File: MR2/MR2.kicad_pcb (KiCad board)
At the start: 2 copper layers, 14 parts, among them J1 Conn_01x04_Male, J2 Conn_01x04_Male, J3 Conn_01x04_Male, J4 Conn_01x04_Male, J5 Conn_01x02_Male, Q1 2SC1815, U5 LPC1768, U6 MPU6050, U7 R3008SB, U8 MCP2561-E-P

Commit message: update:MR2の基板完成
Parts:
- removed Q1: 2SC1815, Package_TO_SOT_THT:TO-92_Inline
- removed R1, R3: R, Resistor_THT:R_Axial_DIN0207_L6.3mm_D2.5mm_P7.62mm_Horizontal
- removed REF**: universal_B, MyFootprint:universal_B
- removed U6: MPU6050, MyFootprint:MPU6050
- removed U7: R3008SB, MyFootprint:R3008SB
- added J6: Conn_01x02_Male, Connector_JST:JST_XH_S2B-XH-A_1x02_P2.50mm_Horizontal, F.Cu at (109.2, 96.6)
- added J7: Conn_01x04_Male, Connector_JST:JST_XH_S4B-XH-A_1x04_P2.50mm_Horizontal, F.Cu at (108.9, 78.7)
- added J8: Conn_01x02_Male, Connector_JST:JST_XH_S2B-XH-A_1x02_P2.50mm_Horizontal, F.Cu at (108.9, 109.2)
- added J9: Conn_01x02_Male, Connector_JST:JST_XH_S2B-XH-A_1x02_P2.50mm_Horizontal, F.Cu at (109.2, 121.9)
- J5: footprint Connector_JST:JST_XH_B2B-XH-A_1x02_P2.50mm_Vertical -> Connector_JST:JST_XH_S2B-XH-A_1x02_P2.50mm_Horizontal
- moved J5 5.68 mm to (177.8, 73.7), turned to 180 degrees
- moved R2 3.59 mm to (185.4, 68.6)
- moved U8 2.54 mm to (172.7, 88.9)
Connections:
- J1 pad 1: PWM_1 -> +5V
- J1 pad 2: IO_1B -> enc_elevator_b
- J1 pad 3: IO_1A -> enc_elevator_a
- J2 pad 1: PWM_2 -> PWM_1
- J2 pad 2: IO_2B -> IO_1A
- J2 pad 3: IO_2A -> IO_1B
- J3 pad 1: PWM_3 -> +5V
- J3 pad 2: IO_3B -> enc_collect_a
- J3 pad 3: IO_3A -> enc_collect_b
- J4 pad 1: PWM_4 -> PWM_2
- J4 pad 2: IO_4B -> IO_2B
- J4 pad 3: IO_4A -> IO_2A
- U5 pad 14: Serial_rx -> Net-(U5-Pad14)
- U5 pad 17: IO_1A -> enc_elevator_a
- U5 pad 18: IO_1B -> enc_elevator_b
- U5 pad 19: IO_2A -> IO_1A
- U5 pad 20: IO_2B -> IO_1B
- U5 pad 21: IO_3A -> enc_collect_a
- U5 pad 22: IO_3B -> enc_collect_b
- U5 pad 25: PWM_3 -> Net-(U5-Pad25)
- U5 pad 26: PWM_4 -> Net-(U5-Pad26)
- U5 pad 27: IO_4A -> IO_2A
- U5 pad 28: IO_4B -> IO_2B
- U5 pad 5: Net-(U5-Pad5) -> air_1
- U5 pad 6: Net-(U5-Pad6) -> air_2
- U5 pad 7: Net-(U5-Pad7) -> sw1
- U5 pad 8: I2C_sda -> sw2
- U5 pad 9: I2C_scl -> sw3
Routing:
- net GND: track 316.0 -> 257.1 mm, vias 11 -> 3
- net I2C_scl: track 53.5 -> 0.00 mm
- net I2C_sda: track 53.1 -> 0.00 mm
- net PWM_2: track 64.7 -> 16.3 mm, vias 2 -> 0
- net sw3: track 0.00 -> 45.6 mm
- net sw2: track 0.00 -> 41.7 mm
- net +5V: track 142.3 -> 103.4 mm
- net Serial_rx: track 38.4 -> 0.00 mm, vias 2 -> 0
- net sw1: track 0.00 -> 37.4 mm
- net air_1: track 0.00 -> 35.0 mm
- net air_2: track 0.00 -> 34.9 mm
- net IO_3A: track 30.0 -> 0.00 mm
- net IO_3B: track 23.5 -> 0.00 mm
- net enc_elevator_a: track 0.00 -> 22.5 mm
- net IO_4B: track 20.3 -> 0.00 mm, vias 2 -> 0
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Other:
- board outline added: 94 x 71.1 mm

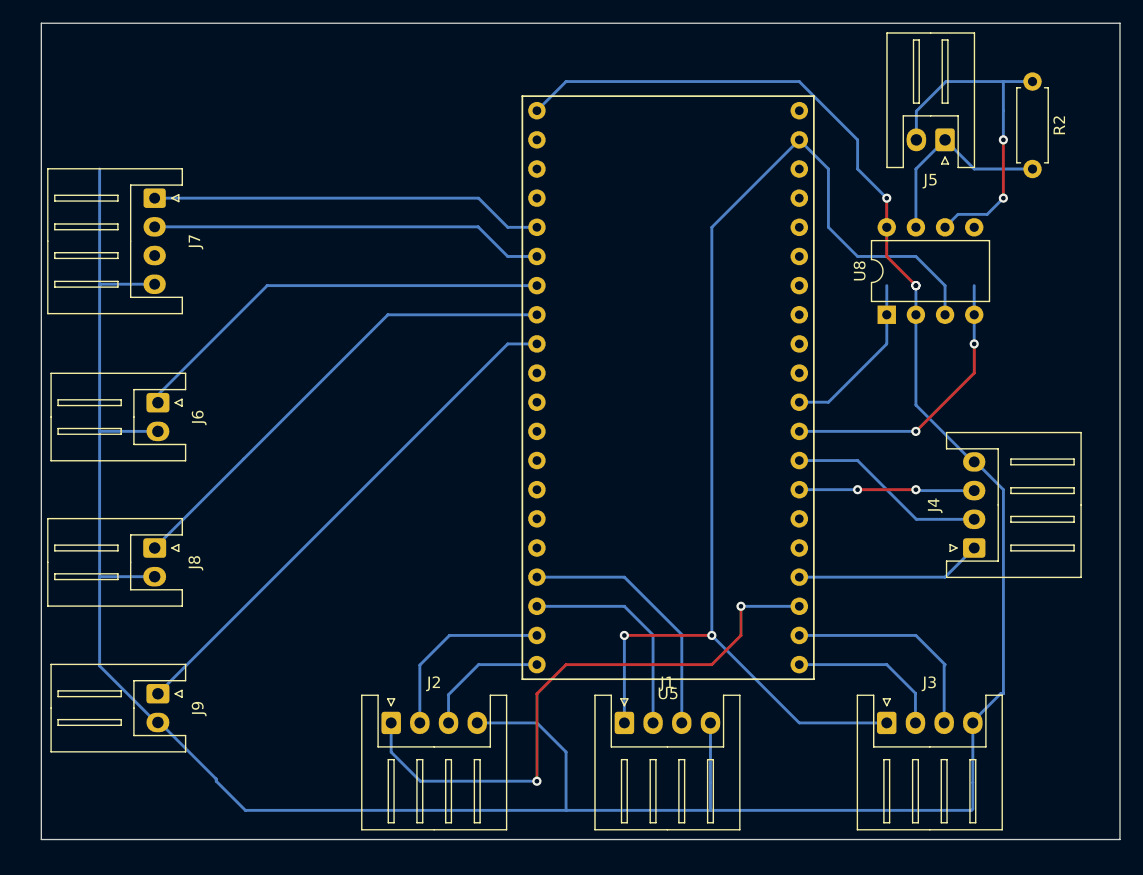
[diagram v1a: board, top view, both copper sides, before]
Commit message: update:設計変更に伴う改修、CAN通信周りの不具合を修正
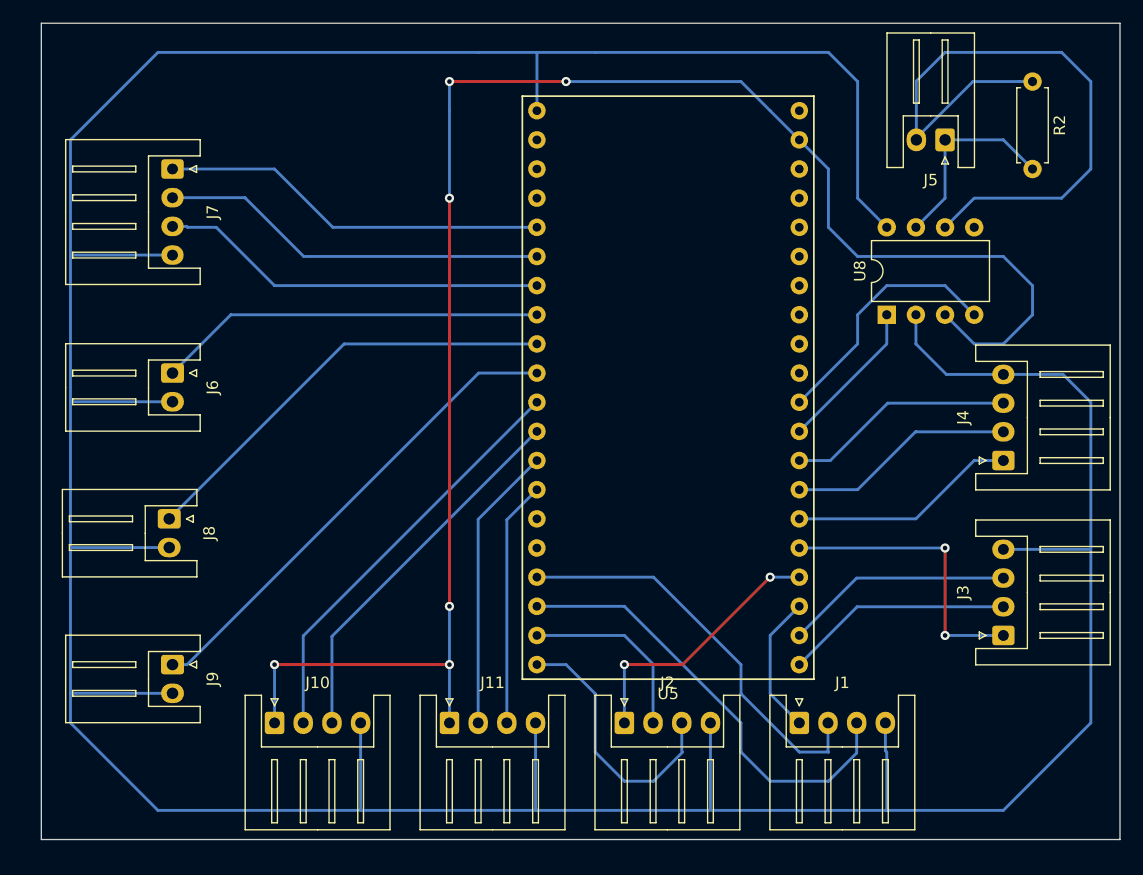
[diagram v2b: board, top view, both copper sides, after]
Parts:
- added J10: Conn_01x04_Male, Connector_JST:JST_XH_S4B-XH-A_1x04_P2.50mm_Horizontal, F.Cu at (119.4, 124.5)
- added J11: Conn_01x04_Male, Connector_JST:JST_XH_S4B-XH-A_1x04_P2.50mm_Horizontal, F.Cu at (134.6, 124.5)
- moved J2 20.3 mm to (149.9, 124.5)
- moved J1 15.2 mm to (165.1, 124.5)
- moved J3 12.7 mm to (182.9, 116.8), turned to 90 degrees
- moved J4 8.03 mm to (182.9, 101.6)
- moved J7 2.98 mm to (110.5, 76.2)
- moved J6 2.88 mm to (110.5, 94.0)
- moved J9 2.84 mm to (110.5, 119.4)
- moved J8 2.84 mm to (110.2, 106.7)
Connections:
- net enc_collect_a renamed IO_3A
- net enc_collect_b renamed IO_3B
- J1 pad 1: +5V -> PWM_1
- J1 pad 2: enc_elevator_b -> IO_1A
- J1 pad 3: enc_elevator_a -> IO_1B
- J2 pad 1: PWM_1 -> PWM_2
- J2 pad 2: IO_1A -> IO_2A
- J2 pad 3: IO_1B -> IO_2B
- J3 pad 1: +5V -> PWM_3
- J4 pad 1: PWM_2 -> PWM_4
- J4 pad 2: IO_2B -> IO_4A
- J4 pad 3: IO_2A -> IO_4B
- J7 pad 3: Net-(J7-Pad3) -> air_3
- U5 pad 10: Net-(U5-Pad10) -> sw3
- U5 pad 11: Net-(U5-Pad11) -> enc_1A
- U5 pad 12: Net-(U5-Pad12) -> enc_1B
- U5 pad 13: Net-(U5-Pad13) -> enc_2A
- U5 pad 14: Net-(U5-Pad14) -> enc_2B
- U5 pad 17: enc_elevator_a -> IO_1A
- U5 pad 18: enc_elevator_b -> IO_1B
- U5 pad 19: IO_1A -> IO_2A
- U5 pad 20: IO_1B -> IO_2B
- U5 pad 25: Net-(U5-Pad25) -> PWM_3
- U5 pad 26: Net-(U5-Pad26) -> PWM_4
- U5 pad 27: IO_2A -> IO_4A
- U5 pad 28: IO_2B -> IO_4B
- U5 pad 29: CAN_rd -> CAN_td
- U5 pad 30: CAN_td -> CAN_rd
- U5 pad 7: sw1 -> air_3
- U5 pad 8: sw2 -> sw1
- U5 pad 9: sw3 -> sw2
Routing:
- net GND: track 257.1 -> 358.8 mm, vias 3 -> 0
- net +5V: track 103.4 -> 149.6 mm, vias 2 -> 6
- net PWM_1: track 51.4 -> 12.3 mm, vias 2 -> 0
- net enc_1A: track 0.00 -> 36.4 mm
- net air_3: track 0.00 -> 33.9 mm
- net enc_1B: track 0.00 -> 32.8 mm
- net IO_1B: track 11.2 -> 39.3 mm
- net CAN_L: track 30.0 -> 57.1 mm, vias 2 -> 0
- net PWM_3: track 0.00 -> 25.4 mm, vias 0 -> 2
- net enc_2A: track 0.00 -> 25.0 mm
- net enc_elevator_a: track 22.5 -> 0.00 mm
- net enc_2B: track 0.00 -> 21.4 mm
- net IO_4A: track 0.00 -> 19.9 mm
- net PWM_4: track 0.00 -> 19.9 mm
- net IO_4B: track 0.00 -> 19.9 mm
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
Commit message: update : mr1:sub_swの追加   mr2:エンコーダーの増設
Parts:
- added J12: Conn_01x04_Male, Connector_JST:JST_XH_S4B-XH-A_1x04_P2.50mm_Horizontal, F.Cu at (129.5, 73.7)
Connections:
- U5 pad 15: Net-(U5-Pad15) -> enc_3A
- U5 pad 16: Net-(U5-Pad16) -> enc_3B
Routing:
- net enc_3B: track 0.00 -> 62.6 mm, vias 0 -> 2
- net enc_3A: track 0.00 -> 52.5 mm, vias 0 -> 2
- net GND: track 358.8 -> 370.2 mm
- net +5V: track 149.6 -> 154.7 mm
- net enc_2A: track 25.0 -> 25.1 mm, vias 0 -> 2
- net enc_2B: vias 0 -> 2
